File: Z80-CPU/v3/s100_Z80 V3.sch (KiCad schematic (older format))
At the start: 166 parts, among them K1 CONN_3, K10 U15 Clock, K2 CONN_3, K3 pSYNCdata, K4 CONN_3, K5 pSYNC, K6 U35p12, K7 U40p8, K8 WRstrobe, K9 U29B Q, P1 S100_MALE, P2 CONN_4X2, P3 CLK_CPU, P34 CONN_1, P35 CONN_1, P36 CONN_3X2, P4 CONN_2X2, P5 CLK_CPU, P6 MASTER_OSC, P7 CLK_SEL, Q1 2N3904, Q2 ^^NPN-SOT23, Q3 ^^NPN-SOT23, Q4 ^^NPN-SOT23, Q5 ^^NPN-SOT23, Q6 ^^NPN-SOT23, Q7 ^^NPN-SOT23, SW1 DIPS_08, SW2 DIPS_08, SW3 DIPS_08, SW4 DIPS_08, U1 Z80, U10 74LS165, U11 74LS165, U12 ^^74LS541, U13 2732, U14 74LS682N, U15 74LS165, U16 74LS273, U17 74LS273, U18 74LS161, U19 ^^74LS541, U2 ^^74LS541, U20 ^^74LS541, U21 ^^74LS541, U22 ^^74LS541, U23 74LS02, U24 74LS04, U25 74LS04, U26 74LS05, U27 74LS139, U28 74LS00, U29 74LS74, U3 ^^74LS541, U31 74LS00, U33 74LS74, U34 74LS74, U35 74LS32, U36 74LS04, U37 74LS05, U38 74F04, U39 74S08, U4 74LS153, U40 74S00, U43 74LS11, U44 74LS32, U45 74LS02, U47 74LS04, U48 LDO_REG_7805, U49 74LS00, U5 74LS157, U6 74LS153, U7 74LS32, U8 74LS157, U9 74LS165

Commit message: Z80-CPU v3: schematic and placement rework
Source: S100 Z80 version3/backups/17-07-2014 0138
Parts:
- removed C42: 22 uF, C1V7, symbol CP
- removed C43: 33 uF, C1V7, symbol CP
- removed C48, C63, C7: 0.1 uF, C2, symbol C
- removed D6: 1N4148, D3, symbol DIODE
- removed JP4, JP5, JP6, JP7: JUMPER, SIL-2, symbol JUMPER
- removed Q1: 2N3904, TO92-INVERT, symbol NPN
- removed R11: 4700, R3, symbol R
- removed RR8, RR9: 1000, r_pack9, symbol RR9
- removed U26: 74LS05, 14dip300, symbol 74LS05
- removed U39: 74S08, 14dip300, symbol 74LS08
- removed U44: 74LS32, ~, symbol 74LS32
- removed U49: 74LS00, 14dip300, symbol 74LS00
- added K11: bA13, SIL-3, symbol CONN_3
- added K12: bA12, SIL-3, symbol CONN_3
- added K13: bA19, SIL-3, symbol CONN_3
- added K14: bA18, SIL-3, symbol CONN_3
- added K15: bA16, SIL-3, symbol CONN_3
- added K16: bA17, SIL-3, symbol CONN_3
- added U39: 74LS02, 14dip300, symbol 74LS02
- K6: value U35p12 -> bA15
- K7: value U40p8 -> bA14
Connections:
- net labels added: IORQ+, MREQ+, MWRTb, RESET*b, pWR*b, sINTAb, sMEMRb, sOUTb
- net labels removed: CLK, IO_WAIT, M1_WAIT, MEM_RD, MEM_WAIT, PU1K-BB, PU1K-CC, PU1K-DD, PU1K-EE, PU1K-FF, PU1K-GG, PU1K-HH, PU1K-I, PU1K-II, PU1K-L, PU1K-O, PU1K-P, PU1K-Q, PU1K-U, PU1K-V, PU1K-W, PU1K-X, PU1K-Z, PU5K-F, PU5K-G, PU5K-I, REFSH+
- wire segments 1352 -> 1248
- no-connect marks 38 -> 36
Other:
- note added: "pSYNC"
- moved on the sheet: K1, R5, RR6, U22, U24B, U25B, U25F, U31A, U35A, U35D, U36B, U36E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

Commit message: Z80-CPU v3: schematic and placement
Source: S100 Z80 version3/backups/17-07-2014 1631
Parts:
- added D8: D2-1, symbol LED
- added K17: EN_WAITS, SIL-3, symbol CONN_3
- added R4: 330, symbol R
- D9: renamed from D8; value POWER -> D2-1
- renumbered R4 to R42
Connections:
- net labels added: PU1K-cp1, PU1K-cp2, PU1K-waits
- wire segments 1248 -> 1265
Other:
- moved on the sheet: D9, R42

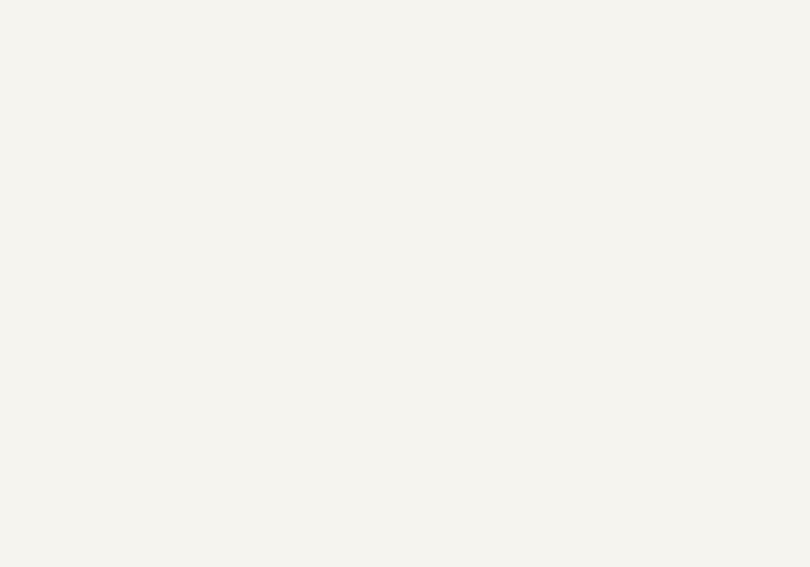
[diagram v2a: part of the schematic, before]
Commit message: Z80-CPU v3: routed REV 2.0 board and gerbers
Source: S100 Z80 version3/backups/20-07-2014
Newest file is 2014-07-18 00:18 (the gerber time); the folder name says 20-07.
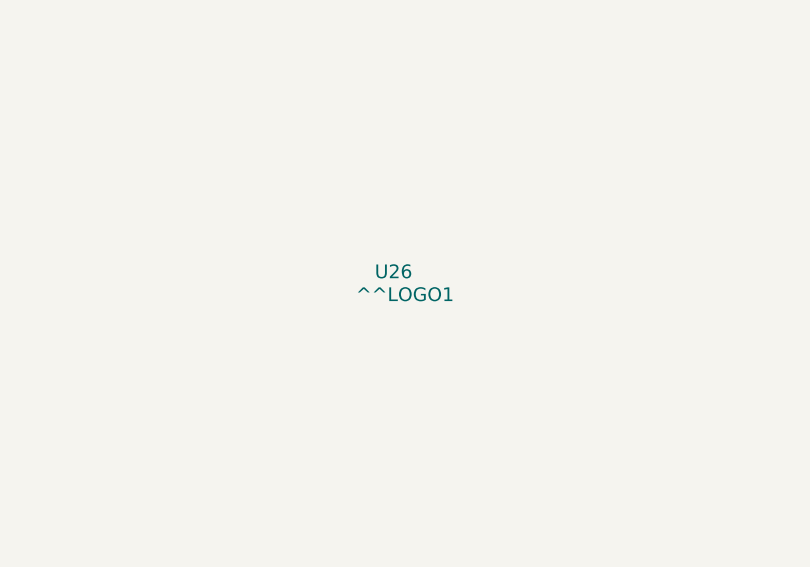
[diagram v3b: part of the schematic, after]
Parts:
- added U26: ^^LOGO1, ~, symbol ^^LOGO1

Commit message: Z80-CPU v3: schematic changes after the gerbers (unrouted board)
Source: S100 Z80 version3/backups/20-07-2014 1447
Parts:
- removed U43: 74LS11, 14dip300, symbol 74LS11
- removed U47: 74LS04, 14dip300, symbol 74LS04
- added C5: 0.1 uF, C2, symbol C
- added K18: ROM_E-, SIL-3, symbol CONN_3
- added R11, R16: 10K, symbol R
- added unit 3 of U24
- added unit 2 of U28
- added U30, U32, U41: ^^74LS541, ~, symbol ^^74LS541
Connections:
- net labels added: ROM_E-
- wire segments 1265 -> 1332
- no-connect marks 36 -> 35
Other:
- note added: "3 input AND"
- moved on the sheet: U13, U25F, U31A, U36A, U36C

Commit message: Z80-CPU v3: schematic trimmed, re-placement
Source: S100 Z80 version3/backups/24-07-2014 end of day
Newest file is 2014-07-23 14:45; the folder name says 24-07.
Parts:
- removed C16, C24, C29, C5, C53, C58: 0.1 uF, C2, symbol C
- removed C6: 0.022 uF, C1V7, symbol CP
- removed D3, D4, D5, D7: DONE, symbol LED
- removed D9: D2-1, symbol LED
- removed Q2, Q3, Q4, Q5, Q6, Q7: ^^NPN-SOT23, ~, symbol ^^NPN-SOT23
- removed R10, R13, R15, R8: 470, symbol R
- removed R12, R14, R42, R9: 330, symbol R
- removed U16, U17: 74LS273, 20dip300, symbol 74LS273
- removed U23: 74LS02, 14dip300, symbol 74LS02
- removed unit 3 of U25
- removed U4, U6: 74LS153, 16dip300, symbol 74LS153
- removed U5: 74LS157, 16dip300, symbol 74LS157
- added P8, P9: CONN_20, symbol CONN_20
- added Q2, Q3: NPN, symbol NPN
- R7: value 330 -> 1K
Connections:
- net labels added: U4p7, U4p9, U5p12, U5p4, U5p7, U5p9, U6p7, U6p9, clkU16, clkU17
- net labels removed: IORQ, RR4p10
- wire segments 1332 -> 1147
- no-connect marks 35 -> 33
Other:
- note removed: "A16"
- note removed: "A17"
- note removed: "A18"
- note removed: "A19"
- moved on the sheet: K13, K14, K15, K16

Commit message: Z80-CPU v3: schematic and placement
Source: S100 Z80 version3/backups/27-07-2014 1407
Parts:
- added D3: WAIT, symbol LED
- added Q1: NPN, symbol NPN
- added R8: 330, symbol R
- added R9: 470, symbol R
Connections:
- net labels added: NMI*s100, ROM_E-33, WAIT+, sWO*b
- wire segments 1147 -> 1182
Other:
- note added: "Z80 WAIT"
- moved on the sheet: P8, P9, U35D, U45B

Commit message: Z80-CPU v3: final schematic and routed board
Source: S100 Z80 version3/backups/S100 Z80 version3 (a full copy of the v3 working folder as of 2014-08-09; its nested backups are the same as the ones already committed).
The gerbers are still the 2014-07-18 set, made before the July 20-26 changes.
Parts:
- U32: value ^^74LS541 -> 74HCT541
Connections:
- wire segments 1182 -> 1181
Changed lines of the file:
@@
 Sheet 1 1
 Title "noname.sch"
-Date "26 jul 2014"
+Date "8 aug 2014"
 Rev ""
 Comp ""
@@
 	36050 30300 36050 32100
 Wire Wire Line
-	36050 32100 37000 32100
-Wire Wire Line
-	37000 32100 37000 32050
-Wire Wire Line
 	36300 31200 36050 31200
 Connection ~ 36050 31200
@@
 	34500 30850 34650 30850
 Wire Wire Line
-	36300 31600 35350 31600
-Wire Wire Line
-	35350 31600 35350 31800
+	35350 31500 35350 31800
 Text Notes 31700 29550 0    60   ~ 0
 MASTER TTL OSCILLATOR
@@
 P 15950 1650
 F 0 "U32" H 15950 2225 60  0000 C BNN
-F 1 "^^74LS541" H 15950 1075 60  0000 C TNN
+F 1 "74HCT541" H 16000 1300 60  0000 C TNN
 F 2 "~" H 15950 1650 60  0000 C CNN
 F 3 "~" H 15950 1650 60  0000 C CNN
@@
 Wire Wire Line
 	10350 3100 9950 3100
+Wire Wire Line
+	36300 31500 35350 31500
+Wire Wire Line
+	36300 31700 36050 31700
+Connection ~ 36050 31700
 $EndSCHEMATC
